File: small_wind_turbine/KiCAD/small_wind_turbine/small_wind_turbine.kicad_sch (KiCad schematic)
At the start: 94 parts, among them J1 Conn_01x03_Male, J2 Conn_01x03_Male, J3 Conn_01x03_Male, K1 G5LE-1, Q1 Q_NMOS_GDS, SW1 SW_Push_SPDT, U10 AZ1117-5.0, U2 UC2844A, U3 LTC4440ES6, U4 Opamp_Quad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

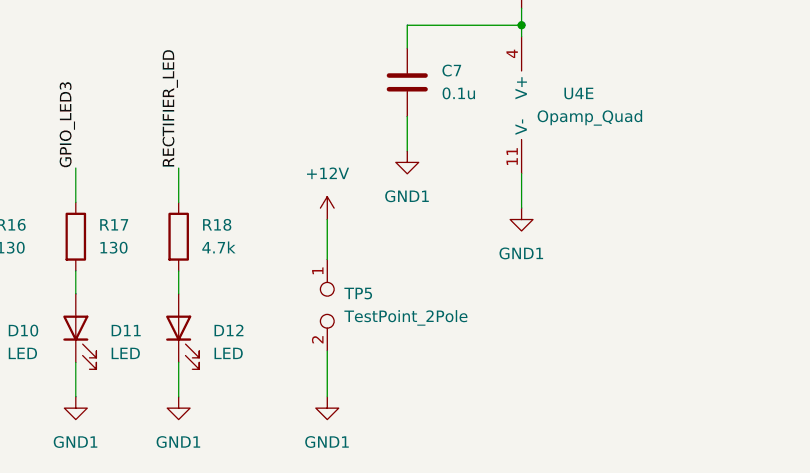
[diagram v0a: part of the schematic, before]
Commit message: move test points close to proper locations
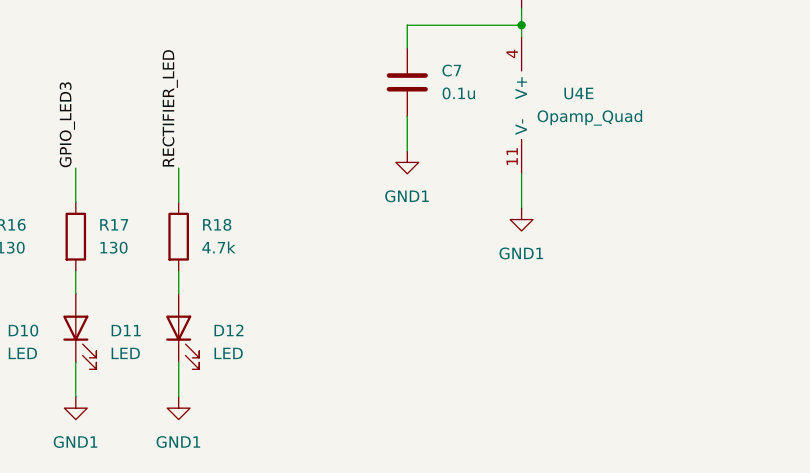
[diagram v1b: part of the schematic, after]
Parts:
- removed TP5: TestPoint_2Pole, small_wind_turbine:Oscilloscope_Test_Point, symbol Connector:TestPoint_2Pole
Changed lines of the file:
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@@
     (stroke (width 0) (type default) (color 0 0 0 0))
   )
-  (wire (pts (xy 104.14 255.905) (xy 104.14 260.35))
-    (stroke (width 0) (type default) (color 0 0 0 0))
-  )
   (wire (pts (xy 160.02 168.91) (xy 160.02 182.88))
     (stroke (width 0) (type default) (color 0 0 0 0))
@@
     (stroke (width 0) (type default) (color 0 0 0 0))
   )
-  (wire (pts (xy 104.14 270.51) (xy 104.14 275.59))
-    (stroke (width 0) (type default) (color 0 0 0 0))
-  )
   (text "Bootstrap Gate Driver" (at 129.54 201.93 0)
     (effects (font (size 3 3)) (justify left bottom))
@@
     (pin "1")
   )
-  (symbol (lib_id "power:+12V") (at 104.14 255.905 0) (unit 1)
-    (in_bom yes) (on_board yes) (fields_autoplaced)
-    (property "Reference" "#PWR052" (id 0) (at 104.14 259.715 0)
-      (effects (font (size 1.27 1.27)) hide)
-    )
-    (property "Value" "+12V" (id 1) (at 104.14 250.825 0))
-    (property "Footprint" "" (id 2) (at 104.14 255.905 0)
-      (effects (font (size 1.27 1.27)) hide)
-    )
-    (property "Datasheet" "" (id 3) (at 104.14 255.905 0)
-      (effects (font (size 1.27 1.27)) hide)
-    )
-    (pin "1")
-  )
   (symbol (lib_id "Device:C") (at 331.47 40.64 0) (unit 1)
     (in_bom yes) (on_board yes)
@@
     (pin "2")
   )
-  (symbol (lib_id "Connector:TestPoint_2Pole") (at 104.14 265.43 270) (unit 1)
-    (in_bom yes) (on_board yes) (fields_autoplaced)
-    (property "Reference" "TP5" (id 0) (at 106.045 264.1599 90)
-      (effects (font (size 1.27 1.27)) (justify left))
-    )
-    (property "Value" "TestPoint_2Pole" (id 1) (at 106.045 266.6999 90)
-      (effects (font (size 1.27 1.27)) (justify left))
-    )
-    (property "Footprint" "small_wind_turbine:Oscilloscope_Test_Point" (id 2) (at 104.14 265.43 0)
-      (effects (font (size 1.27 1.27)) hide)
-    )
-    (property "Datasheet" "~" (id 3) (at 104.14 265.43 0)
-      (effects (font (size 1.27 1.27)) hide)
-    )
-    (pin "1")
-    (pin "2")
-  )
   (symbol (lib_id "Connector:Screw_Terminal_01x02") (at 131.445 63.5 270) (unit 1)
     (in_bom yes) (on_board yes) (fields_autoplaced)
@@
     (pin "1")
   )
-  (symbol (lib_id "power:GND1") (at 104.14 275.59 0) (unit 1)
-    (in_bom yes) (on_board yes) (fields_autoplaced)
-    (property "Reference" "#PWR053" (id 0) (at 104.14 281.94 0)
-      (effects (font (size 1.27 1.27)) hide)
-    )
-    (property "Value" "GND1" (id 1) (at 104.14 280.67 0))
-    (property "Footprint" "" (id 2) (at 104.14 275.59 0)
-      (effects (font (size 1.27 1.27)) hide)
-    )
-    (property "Datasheet" "" (id 3) (at 104.14 275.59 0)
-      (effects (font (size 1.27 1.27)) hide)
-    )
-    (pin "1")
-  )
   (symbol (lib_id "Device:C") (at 238.76 96.52 90) (unit 1)
     (in_bom yes) (on_board yes) (fields_autoplaced)
@@
       (reference "#PWR051") (unit 1) (value "GND1") (footprint "")
     )
-    (path "/12f1248c-4694-4782-ab77-ae3088012281"
-      (reference "#PWR052") (unit 1) (value "+12V") (footprint "")
-    )
-    (path "/7cdf800a-a6db-41c2-a3ac-ff063b806555"
-      (reference "#PWR053") (unit 1) (value "GND1") (footprint "")
-    )
     (path "/3eadf22a-3e98-4263-a3df-8d877a19603f"
       (reference "#PWR054") (unit 1) (value "GND1") (footprint "")
@@
       (reference "TP4") (unit 1) (value "TestPoint_2Pole") (footprint "small_wind_turbine:Oscilloscope_Test_Point")
     )
-    (path "/19548b00-592b-457a-8512-e19cf941ccdb"
-      (reference "TP5") (unit 1) (value "TestPoint_2Pole") (footprint "small_wind_turbine:Oscilloscope_Test_Point")
-    )
     (path "/f593b037-3443-4963-ac1e-f5222fe40392"

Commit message: finalize relative positions; ready to start finessing
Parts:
- removed TP7: TestPoint_2Pole, small_wind_turbine:Oscilloscope_Test_Point, symbol Connector:TestPoint_2Pole
- Jbat1, Jres1: footprint TerminalBlock_Phoenix:TerminalBlock_Phoenix_MKDS-1,5-2-5.08_1x02_P5.08mm_Horizontal -> small_wind_turbine:TerminalBlock_1x02_P5.08mm_leads
- Jgen1: footprint TerminalBlock_Phoenix:TerminalBlock_Phoenix_MKDS-1,5-3-5.08_1x03_P5.08mm_Horizontal -> small_wind_turbine:TerminalBlock_1x03_P5.08mm_Horizontal
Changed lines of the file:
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@@
   (junction (at 131.445 55.245) (diameter 0) (color 0 0 0 0)
   )
-  (junction (at 161.29 123.19) (diameter 0) (color 0 0 0 0)
-  )
   (junction (at 40.64 101.6) (diameter 0) (color 0 0 0 0)
   )
@@
   (junction (at 173.99 123.19) (diameter 0) (color 0 0 0 0)
   )
-  (junction (at 161.29 101.6) (diameter 0) (color 0 0 0 0)
-  )
   (junction (at 131.445 101.6) (diameter 0) (color 0 0 0 0)
   )
@@
     (stroke (width 0) (type default) (color 0 0 0 0))
   )
-  (wire (pts (xy 157.48 101.6) (xy 161.29 101.6))
-    (stroke (width 0) (type default) (color 0 0 0 0))
-  )
   (polyline (pts (xy 190.5 17.78) (xy 190.5 72.39))
     (stroke (width 0) (type default) (color 0 0 0 0))
@@
     (stroke (width 0) (type default) (color 0 0 0 0))
   )
-  (wire (pts (xy 161.29 123.19) (xy 166.37 123.19))
-    (stroke (width 0) (type default) (color 0 0 0 0))
-  )
   (wire (pts (xy 243.84 163.83) (xy 243.84 167.64))
     (stroke (width 0) (type default) (color 0 0 0 0))
@@
     (stroke (width 0) (type default) (color 0 0 0 0))
   )
-  (wire (pts (xy 161.29 101.6) (xy 166.37 101.6))
+  (wire (pts (xy 157.48 101.6) (xy 166.37 101.6))
     (stroke (width 0) (type default) (color 0 0 0 0))
   )
@@
     (stroke (width 0) (type default) (color 0 0 0 0))
   )
-  (wire (pts (xy 137.16 123.19) (xy 161.29 123.19))
+  (wire (pts (xy 137.16 123.19) (xy 166.37 123.19))
     (stroke (width 0) (type default) (color 0 0 0 0))
   )
@@
     (stroke (width 0) (type default) (color 0 0 0 0))
   )
-  (wire (pts (xy 161.29 101.6) (xy 161.29 107.95))
-    (stroke (width 0) (type default) (color 0 0 0 0))
-  )
   (wire (pts (xy 144.78 90.17) (xy 144.78 101.6))
     (stroke (width 0) (type default) (color 0 0 0 0))
@@
     (stroke (width 0) (type default) (color 0 0 0 0))
   )
-  (wire (pts (xy 161.29 118.11) (xy 161.29 123.19))
-    (stroke (width 0) (type default) (color 0 0 0 0))
-  )
   (wire (pts (xy 156.21 35.56) (xy 156.21 34.29))
     (stroke (width 0) (type default) (color 0 0 0 0))
@@
     (pin "2")
   )
-  (symbol (lib_id "Connector:TestPoint_2Pole") (at 161.29 113.03 270) (unit 1)
-    (in_bom yes) (on_board yes)
-    (property "Reference" "TP7" (id 0) (at 154.94 116.205 90)
-      (effects (font (size 1.27 1.27)) (justify left))
-    )
-    (property "Value" "TestPoint_2Pole" (id 1) (at 144.78 119.38 90)
-      (effects (font (size 1.27 1.27)) (justify left))
-    )
-    (property "Footprint" "small_wind_turbine:Oscilloscope_Test_Point" (id 2) (at 161.29 113.03 0)
-      (effects (font (size 1.27 1.27)) hide)
-    )
-    (property "Datasheet" "~" (id 3) (at 161.29 113.03 0)
-      (effects (font (size 1.27 1.27)) hide)
-    )
-    (pin "1")
-    (pin "2")
-  )
   (symbol (lib_id "Device:C") (at 337.82 40.64 0) (unit 1)
     (in_bom yes) (on_board yes)
@@
       (effects (font (size 1.27 1.27)) (justify left))
     )
-    (property "Footprint" "TerminalBlock_Phoenix:TerminalBlock_Phoenix_MKDS-1,5-2-5.08_1x02_P5.08mm_Horizontal" (id 2) (at 131.445 63.5 0)
+    (property "Footprint" "small_wind_turbine:TerminalBlock_1x02_P5.08mm_leads" (id 2) (at 131.445 63.5 0)
       (effects (font (size 1.27 1.27)) hide)
     )
@@
     (property "Reference" "Jgen1" (id 0) (at 31.115 30.48 0))
     (property "Value" "Screw_Terminal_01x03" (id 1) (at 31.115 33.02 0))
-    (property "Footprint" "TerminalBlock_Phoenix:TerminalBlock_Phoenix_MKDS-1,5-3-5.08_1x03_P5.08mm_Horizontal" (id 2) (at 31.115 39.37 0)
+    (property "Footprint" "small_wind_turbine:TerminalBlock_1x03_P5.08mm_Horizontal" (id 2) (at 31.115 39.37 0)
       (effects (font (size 1.27 1.27)) hide)
     )
@@
       (effects (font (size 1.27 1.27)) (justify left))
     )
-    (property "Footprint" "TerminalBlock_Phoenix:TerminalBlock_Phoenix_MKDS-1,5-2-5.08_1x02_P5.08mm_Horizontal" (id 2) (at 171.45 111.76 0)
+    (property "Footprint" "small_wind_turbine:TerminalBlock_1x02_P5.08mm_leads" (id 2) (at 171.45 111.76 0)
       (effects (font (size 1.27 1.27)) hide)
     )
@@
     )
     (path "/c346af4d-70e6-4239-ae69-840d06e1dca9"
-      (reference "Jbat1") (unit 1) (value "Screw_Terminal_01x02") (footprint "TerminalBlock_Phoenix:TerminalBlock_Phoenix_MKDS-1,5-2-5.08_1x02_P5.08mm_Horizontal")
+      (reference "Jbat1") (unit 1) (value "Screw_Terminal_01x02") (footprint "small_wind_turbine:TerminalBlock_1x02_P5.08mm_leads")
     )
     (path "/41d6540c-26d7-4e6c-8fd9-d4bf0dfeb44c"
-      (reference "Jgen1") (unit 1) (value "Screw_Terminal_01x03") (footprint "TerminalBlock_Phoenix:TerminalBlock_Phoenix_MKDS-1,5-3-5.08_1x03_P5.08mm_Horizontal")
+      (reference "Jgen1") (unit 1) (value "Screw_Terminal_01x03") (footprint "small_wind_turbine:TerminalBlock_1x03_P5.08mm_Horizontal")
     )
     (path "/1ab67915-2950-455d-892b-4754085f1747"
-      (reference "Jres1") (unit 1) (value "Screw_Terminal_01x02") (footprint "TerminalBlock_Phoenix:TerminalBlock_Phoenix_MKDS-1,5-2-5.08_1x02_P5.08mm_Horizontal")
+      (reference "Jres1") (unit 1) (value "Screw_Terminal_01x02") (footprint "small_wind_turbine:TerminalBlock_1x02_P5.08mm_leads")
     )
     (path "/d6fe864f-55c9-4e92-95b4-f639ead47694"
@@
       (reference "TP6") (unit 1) (value "TestPoint_2Pole") (footprint "small_wind_turbine:Oscilloscope_Test_Point")
     )
-    (path "/098565ad-d23a-4022-a826-74e538247568"
-      (reference "TP7") (unit 1) (value "TestPoint_2Pole") (footprint "small_wind_turbine:Oscilloscope_Test_Point")
-    )
     (path "/c2ec9c23-2f01-436b-ae17-b487ea896379"

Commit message: replace terminal blocks and add silkscreen design
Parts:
- K1: footprint Relay_THT:Relay_SPDT_Omron-G5LE-1 -> small_wind_turbine:Relay_SPDT_Omron_G5LE-1
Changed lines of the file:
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@@
     (property "Reference" "K1" (id 0) (at 116.205 24.13 90))
     (property "Value" "G5LE-1" (id 1) (at 116.205 26.67 90))
-    (property "Footprint" "Relay_THT:Relay_SPDT_Omron-G5LE-1" (id 2) (at 114.935 50.8 0)
+    (property "Footprint" "small_wind_turbine:Relay_SPDT_Omron_G5LE-1" (id 2) (at 114.935 50.8 0)
       (effects (font (size 1.27 1.27)) (justify left) hide)
     )
@@
     )
     (path "/d6fe864f-55c9-4e92-95b4-f639ead47694"
-      (reference "K1") (unit 1) (value "G5LE-1") (footprint "Relay_THT:Relay_SPDT_Omron-G5LE-1")
+      (reference "K1") (unit 1) (value "G5LE-1") (footprint "small_wind_turbine:Relay_SPDT_Omron_G5LE-1")
     )
     (path "/97263c60-67a3-4e83-aaf1-37328c6615bf"

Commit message: add 3d models and fix transistor pin ordering
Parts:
- F1: footprint small_wind_turbine:5x20mm_fuse_holder -> small_wind_turbine:FUSE_4527
- Jbat1, Jres1: footprint small_wind_turbine:TerminalBlock_1x02_P5.08mm_leads -> small_wind_turbine:CUI_TBP01R1-508-02BE
- Jgen1: footprint small_wind_turbine:TerminalBlock_1x03_P5.08mm_Horizontal -> small_wind_turbine:CUI_TBP01R1-508-03BE
- Qbuck1: symbol Device:Q_NMOS_GDS -> Device:Q_NMOS_GSD
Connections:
- net GATE_SOURCE: now also Qbuck1.3 (D); no longer Qbuck1.2 (D)
- net RECTIFIER_VDD: now also Qbuck1.2 (S); no longer Qbuck1.3 (S)
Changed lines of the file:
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@@
       (effects (font (size 1.27 1.27)) (justify left))
     )
-    (property "Footprint" "small_wind_turbine:TerminalBlock_1x02_P5.08mm_leads" (id 2) (at 131.445 63.5 0)
+    (property "Footprint" "small_wind_turbine:CUI_TBP01R1-508-02BE" (id 2) (at 131.445 63.5 0)
       (effects (font (size 1.27 1.27)) hide)
     )
@@
     (property "Reference" "F1" (id 0) (at 87.63 20.32 90))
     (property "Value" "1.5A" (id 1) (at 87.63 22.86 90))
-    (property "Footprint" "small_wind_turbine:5x20mm_fuse_holder" (id 2) (at 87.63 27.813 90)
+    (property "Footprint" "small_wind_turbine:FUSE_4527" (id 2) (at 87.63 27.813 90)
       (effects (font (size 1.27 1.27)) hide)
     )
@@
     (property "Reference" "Jgen1" (id 0) (at 31.115 30.48 0))
     (property "Value" "Screw_Terminal_01x03" (id 1) (at 31.115 33.02 0))
-    (property "Footprint" "small_wind_turbine:TerminalBlock_1x03_P5.08mm_Horizontal" (id 2) (at 31.115 39.37 0)
+    (property "Footprint" "small_wind_turbine:CUI_TBP01R1-508-03BE" (id 2) (at 31.115 39.37 0)
       (effects (font (size 1.27 1.27)) hide)
     )
@@
       (effects (font (size 1.27 1.27)) (justify left))
     )
-    (property "Footprint" "small_wind_turbine:TerminalBlock_1x02_P5.08mm_leads" (id 2) (at 171.45 111.76 0)
+    (property "Footprint" "small_wind_turbine:CUI_TBP01R1-508-02BE" (id 2) (at 171.45 111.76 0)
       (effects (font (size 1.27 1.27)) hide)
     )
@@
     (pin "6")
   )
-  (symbol (lib_id "Device:Q_NMOS_GDS") (at 64.135 99.06 270) (unit 1)
+  (symbol (lib_id "Device:Q_NMOS_GSD") (at 64.135 99.06 270) (unit 1)
     (in_bom yes) (on_board yes)
     (property "Reference" "Qbuck1" (id 0) (at 64.135 105.41 90))
@@
     )
     (path "/1e563895-7a76-4dc7-88cd-1d77261b265a"
-      (reference "F1") (unit 1) (value "1.5A") (footprint "small_wind_turbine:5x20mm_fuse_holder")
+      (reference "F1") (unit 1) (value "1.5A") (footprint "small_wind_turbine:FUSE_4527")
     )
     (path "/1afcae1f-c0cc-4366-be46-912755a4a027"
@@
     )
     (path "/c346af4d-70e6-4239-ae69-840d06e1dca9"
-      (reference "Jbat1") (unit 1) (value "Screw_Terminal_01x02") (footprint "small_wind_turbine:TerminalBlock_1x02_P5.08mm_leads")
+      (reference "Jbat1") (unit 1) (value "Screw_Terminal_01x02") (footprint "small_wind_turbine:CUI_TBP01R1-508-02BE")
     )
     (path "/41d6540c-26d7-4e6c-8fd9-d4bf0dfeb44c"
-      (reference "Jgen1") (unit 1) (value "Screw_Terminal_01x03") (footprint "small_wind_turbine:TerminalBlock_1x03_P5.08mm_Horizontal")
+      (reference "Jgen1") (unit 1) (value "Screw_Terminal_01x03") (footprint "small_wind_turbine:CUI_TBP01R1-508-03BE")
     )
     (path "/1ab67915-2950-455d-892b-4754085f1747"
-      (reference "Jres1") (unit 1) (value "Screw_Terminal_01x02") (footprint "small_wind_turbine:TerminalBlock_1x02_P5.08mm_leads")
+      (reference "Jres1") (unit 1) (value "Screw_Terminal_01x02") (footprint "small_wind_turbine:CUI_TBP01R1-508-02BE")
     )
     (path "/d6fe864f-55c9-4e92-95b4-f639ead47694"

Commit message: add jumper to switch 5V rail
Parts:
- added J4: Conn_01x03_Male, Connector_PinHeader_2.54mm:PinHeader_1x03_P2.54mm_Vertical, symbol Connector:Conn_01x03_Male
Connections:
- net +5V: now also J4.2 (Pin_2); no longer A1.26 (USB), U10.2 (VO)
- new net: J4.3 (Pin_3), U10.2 (VO)
- new net: A1.26 (USB), J4.1 (Pin_1)
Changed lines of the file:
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@@
     (stroke (width 0) (type default) (color 0 0 0 0))
   )
+  (wire (pts (xy 369.57 38.1) (xy 369.57 41.91))
+    (stroke (width 0) (type default) (color 0 0 0 0))
+  )
   (wire (pts (xy 248.92 185.42) (xy 248.92 187.96))
     (stroke (width 0) (type default) (color 0 0 0 0))
@@
     (stroke (width 0) (type default) (color 0 0 0 0))
   )
-  (wire (pts (xy 370.84 50.8) (xy 370.84 48.26))
-    (stroke (width 0) (type default) (color 0 0 0 0))
-  )
   (wire (pts (xy 30.48 271.78) (xy 30.48 275.59))
     (stroke (width 0) (type default) (color 0 0 0 0))
@@
     (stroke (width 0) (type default) (color 0 0 0 0))
   )
+  (wire (pts (xy 371.475 30.48) (xy 371.475 27.305))
+    (stroke (width 0) (type default) (color 0 0 0 0))
+  )
   (wire (pts (xy 228.6 215.9) (xy 220.98 215.9))
     (stroke (width 0) (type default) (color 0 0 0 0))
@@
     (stroke (width 0) (type default) (color 0 0 0 0))
   )
-  (wire (pts (xy 365.76 27.94) (xy 365.76 30.48))
-    (stroke (width 0) (type default) (color 0 0 0 0))
-  )
   (wire (pts (xy 174.625 147.955) (xy 174.625 151.765))
     (stroke (width 0) (type default) (color 0 0 0 0))
@@
     (stroke (width 0) (type default) (color 0 0 0 0))
   )
+  (wire (pts (xy 376.555 27.305) (xy 376.555 50.8))
+    (stroke (width 0) (type default) (color 0 0 0 0))
+  )
   (wire (pts (xy 311.15 217.17) (xy 337.82 217.17))
     (stroke (width 0) (type default) (color 0 0 0 0))
@@
     (stroke (width 0) (type default) (color 0 0 0 0))
   )
+  (wire (pts (xy 368.3 50.8) (xy 376.555 50.8))
+    (stroke (width 0) (type default) (color 0 0 0 0))
+  )
   (wire (pts (xy 337.82 48.26) (xy 337.82 44.45))
     (stroke (width 0) (type default) (color 0 0 0 0))
@@
     (stroke (width 0) (type default) (color 0 0 0 0))
   )
-  (wire (pts (xy 368.3 50.8) (xy 370.84 50.8))
-    (stroke (width 0) (type default) (color 0 0 0 0))
-  )
   (wire (pts (xy 243.84 167.64) (xy 243.84 170.18))
     (stroke (width 0) (type default) (color 0 0 0 0))
@@
     (stroke (width 0) (type default) (color 0 0 0 0))
   )
-  (wire (pts (xy 360.68 30.48) (xy 365.76 30.48))
+  (wire (pts (xy 360.68 30.48) (xy 371.475 30.48))
     (stroke (width 0) (type default) (color 0 0 0 0))
   )
@@
     (stroke (width 0) (type default) (color 0 0 0 0))
   )
+  (wire (pts (xy 374.015 27.305) (xy 374.015 41.91))
+    (stroke (width 0) (type default) (color 0 0 0 0))
+  )
   (wire (pts (xy 160.02 194.31) (xy 154.94 194.31))
     (stroke (width 0) (type default) (color 0 0 0 0))
@@
     (stroke (width 0) (type default) (color 0 0 0 0))
   )
+  (wire (pts (xy 369.57 41.91) (xy 374.015 41.91))
+    (stroke (width 0) (type default) (color 0 0 0 0))
+  )
   (wire (pts (xy 91.44 26.035) (xy 99.06 26.035))
     (stroke (width 0) (type default) (color 0 0 0 0))
@@
     (pin "1")
   )
+  (symbol (lib_id "Connector:Conn_01x03_Male") (at 374.015 22.225 270) (unit 1)
+    (in_bom yes) (on_board yes)
+    (property "Reference" "J4" (id 0) (at 374.015 17.145 90))
+    (property "Value" "Conn_01x03_Male" (id 1) (at 376.555 19.685 90))
+    (property "Footprint" "Connector_PinHeader_2.54mm:PinHeader_1x03_P2.54mm_Vertical" (id 2) (at 374.015 22.225 0)
+      (effects (font (size 1.27 1.27)) hide)
+    )
+    (property "Datasheet" "~" (id 3) (at 374.015 22.225 0)
+      (effects (font (size 1.27 1.27)) hide)
+    )
+    (pin "1")
+    (pin "2")
+    (pin "3")
+  )
   (symbol (lib_id "Device:C") (at 331.47 40.64 0) (unit 1)
     (in_bom yes) (on_board yes)
@@
     (pin "1")
   )
-  (symbol (lib_id "power:+5V") (at 370.84 48.26 0) (unit 1)
-    (in_bom yes) (on_board yes)
-    (property "Reference" "#PWR028" (id 0) (at 370.84 52.07 0)
-      (effects (font (size 1.27 1.27)) hide)
-    )
-    (property "Value" "+5V" (id 1) (at 370.84 43.18 0))
-    (property "Footprint" "" (id 2) (at 370.84 48.26 0)
-      (effects (font (size 1.27 1.27)) hide)
-    )
-    (property "Datasheet" "" (id 3) (at 370.84 48.26 0)
-      (effects (font (size 1.27 1.27)) hide)
-    )
-    (pin "1")
-  )
   (symbol (lib_id "power:GND1") (at 87.63 275.59 0) (unit 1)
     (in_bom yes) (on_board yes) (fields_autoplaced)
@@
     (pin "2")
   )
-  (symbol (lib_id "power:+5V") (at 365.76 27.94 0) (unit 1)
+  (symbol (lib_id "power:+5V") (at 369.57 38.1 0) (unit 1)
     (in_bom yes) (on_board yes)
-    (property "Reference" "#PWR032" (id 0) (at 365.76 31.75 0)
+    (property "Reference" "#PWR032" (id 0) (at 369.57 41.91 0)
       (effects (font (size 1.27 1.27)) hide)
     )
-    (property "Value" "+5V" (id 1) (at 365.76 22.86 0))
-    (property "Footprint" "" (id 2) (at 365.76 27.94 0)
+    (property "Value" "+5V" (id 1) (at 369.57 33.02 0))
+    (property "Footprint" "" (id 2) (at 369.57 38.1 0)
       (effects (font (size 1.27 1.27)) hide)
     )
-    (property "Datasheet" "" (id 3) (at 365.76 27.94 0)
+    (property "Datasheet" "" (id 3) (at 369.57 38.1 0)
       (effects (font (size 1.27 1.27)) hide)
     )
@@
       (reference "#PWR027") (unit 1) (value "+3V3") (footprint "")
     )
-    (path "/5e8a7518-3c71-4f26-9bf5-41ae62798c50"
-      (reference "#PWR028") (unit 1) (value "+5V") (footprint "")
-    )
     (path "/a9d65d09-6e3b-4216-bdda-cffd591bd4a0"
       (reference "#PWR029") (unit 1) (value "GND1") (footprint "")
@@
       (reference "J3") (unit 1) (value "Conn_01x03_Male") (footprint "Connector_PinHeader_2.54mm:PinHeader_1x03_P2.54mm_Vertical")
     )
+    (path "/16239a22-140a-4117-afb9-20365872ec8a"
+      (reference "J4") (unit 1) (value "Conn_01x03_Male") (footprint "Connector_PinHeader_2.54mm:PinHeader_1x03_P2.54mm_Vertical")
+    )
     (path "/c346af4d-70e6-4239-ae69-840d06e1dca9"
